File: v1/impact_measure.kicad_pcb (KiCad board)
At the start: 4 copper layers, 30.6 x 20.5 mm, 64 parts, among them Q2 SP2002KNC, SW1 SW_Push, SW2 SW_Push, U2 ESP32-C3FH4, U3 GS2019-33TR5, U4 ADXL375BCCZ, Y1 40MHz

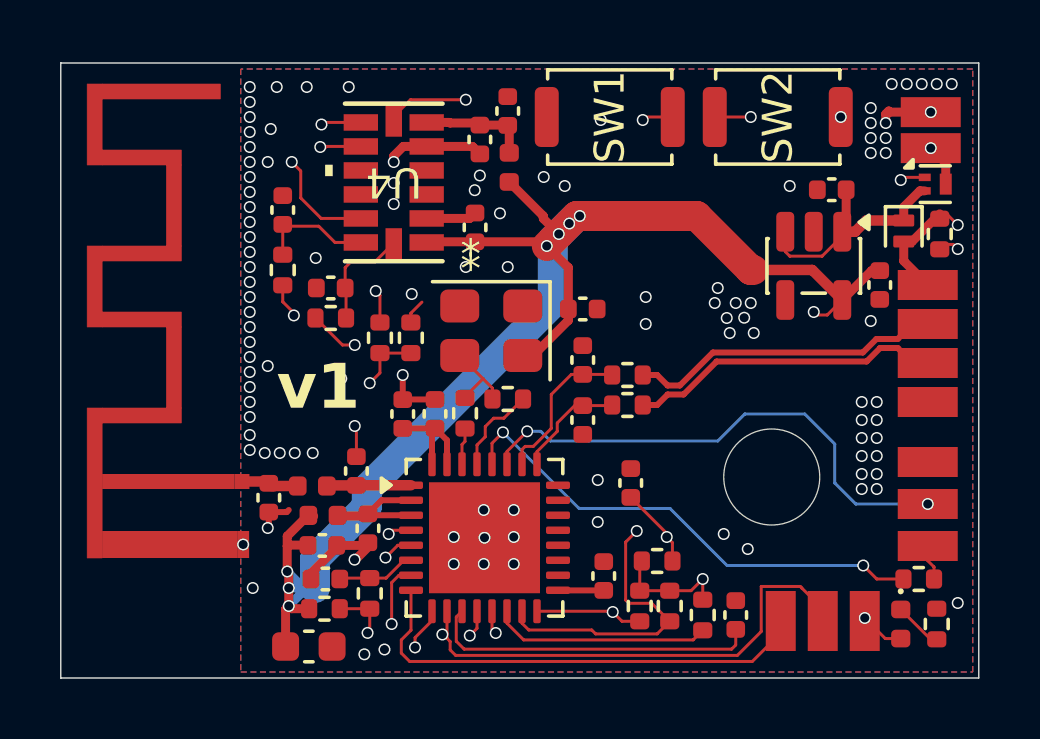
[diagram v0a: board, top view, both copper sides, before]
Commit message: fixed LCSC partnumbers fixed after DRC
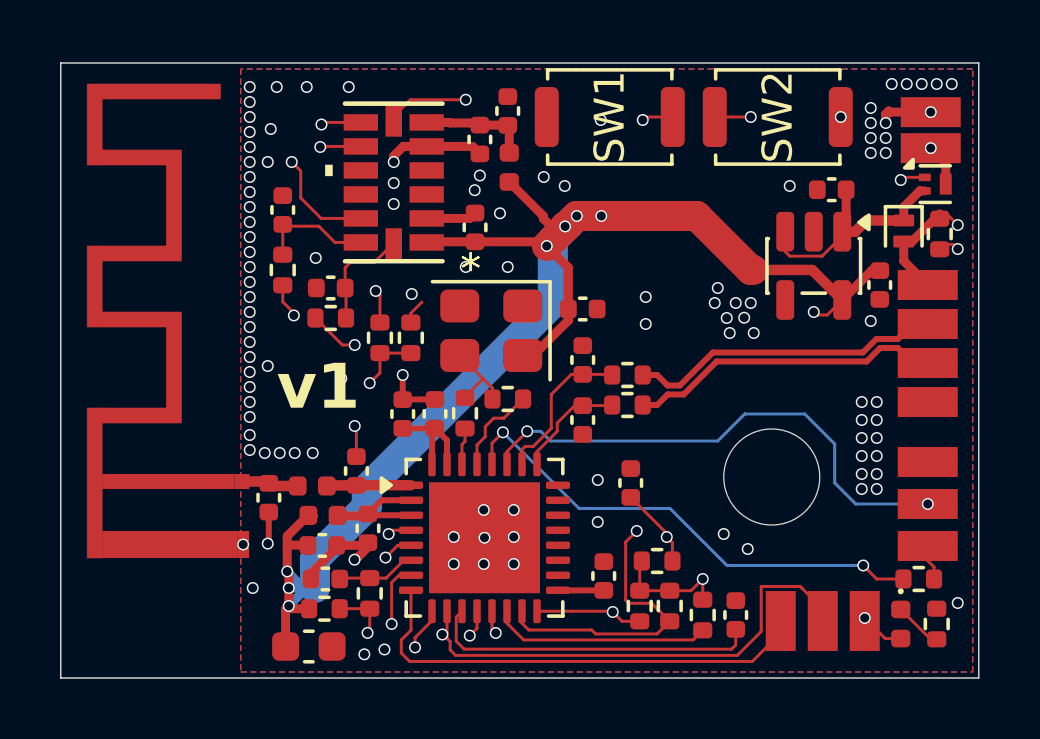
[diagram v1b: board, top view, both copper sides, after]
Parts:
- turned R11 to -90 degrees
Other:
- board text added: "*"

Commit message: added connector for battery
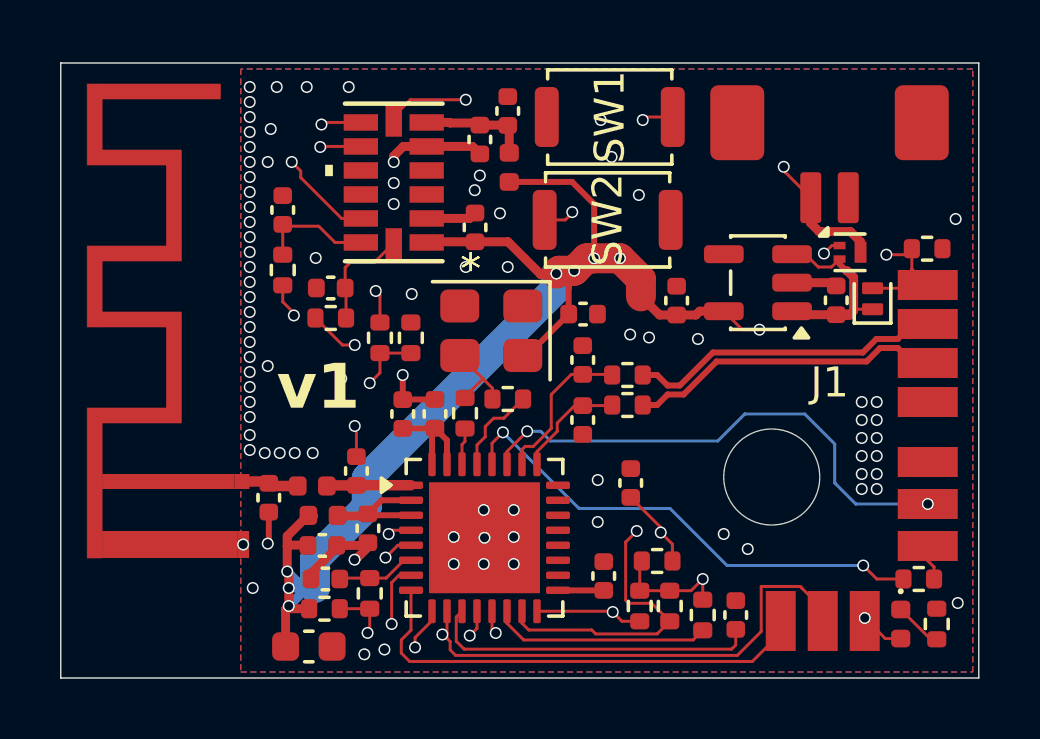
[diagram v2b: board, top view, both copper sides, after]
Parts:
- removed TP11, TP12: TestPoint, Local:TP_1x2mm
- added J1: Bossie BX-MX1.25-2PWT, Local:mx1.25, F.Cu at (100.7, 49.1)
- moved C15 6.79 mm to (95.6, 51.5), turned to 90 degrees
- moved SW2 6.63 mm to (93.3, 48.8)
- moved C14 3.69 mm to (101.0, 51.5), turned to 90 degrees
- moved Q2 3.64 mm to (101.4, 49.9)
- moved D3 2.49 mm to (102.2, 51.5), turned to 90 degrees
- moved U3 1.94 mm to (98.3, 50.9), turned to 180 degrees
- moved R15 0.65 mm to (104.0, 49.8), turned to 180 degrees
- moved C21 0.17 mm to (92.5, 52.0)
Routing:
- net VDD: track 70.1 -> 61.9 mm
- net GND: track 15.5 -> 13.4 mm, vias 109 -> 86
- net VBAT: track 27.7 -> 26.2 mm
- net Net-(D3-K): track 8.08 -> 7.15 mm
- net RESET: track 33.1 -> 33.8 mm
- net VBUS: track 7.48 -> 6.97 mm

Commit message: added vias for gnd fixed after drc
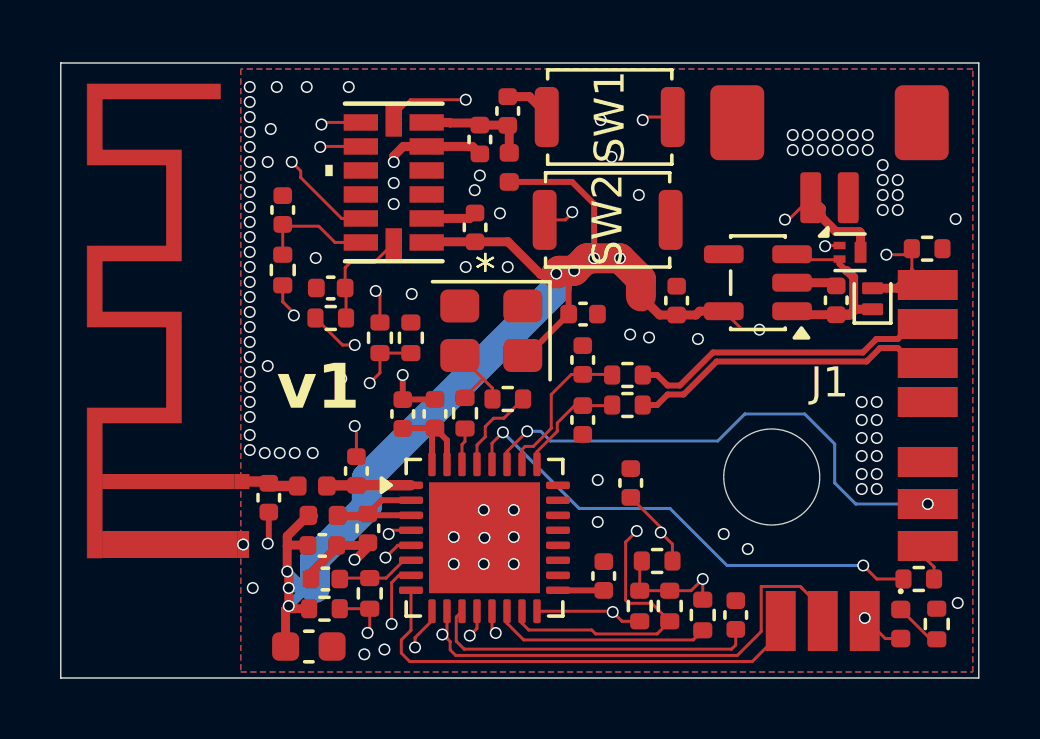
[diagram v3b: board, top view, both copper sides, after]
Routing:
- net GND: track 13.4 -> 15.1 mm, vias 86 -> 105
